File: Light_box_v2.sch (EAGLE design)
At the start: 35 parts, among them IC1 ATMEGA328-PU, U1 OPA1671IDBVR

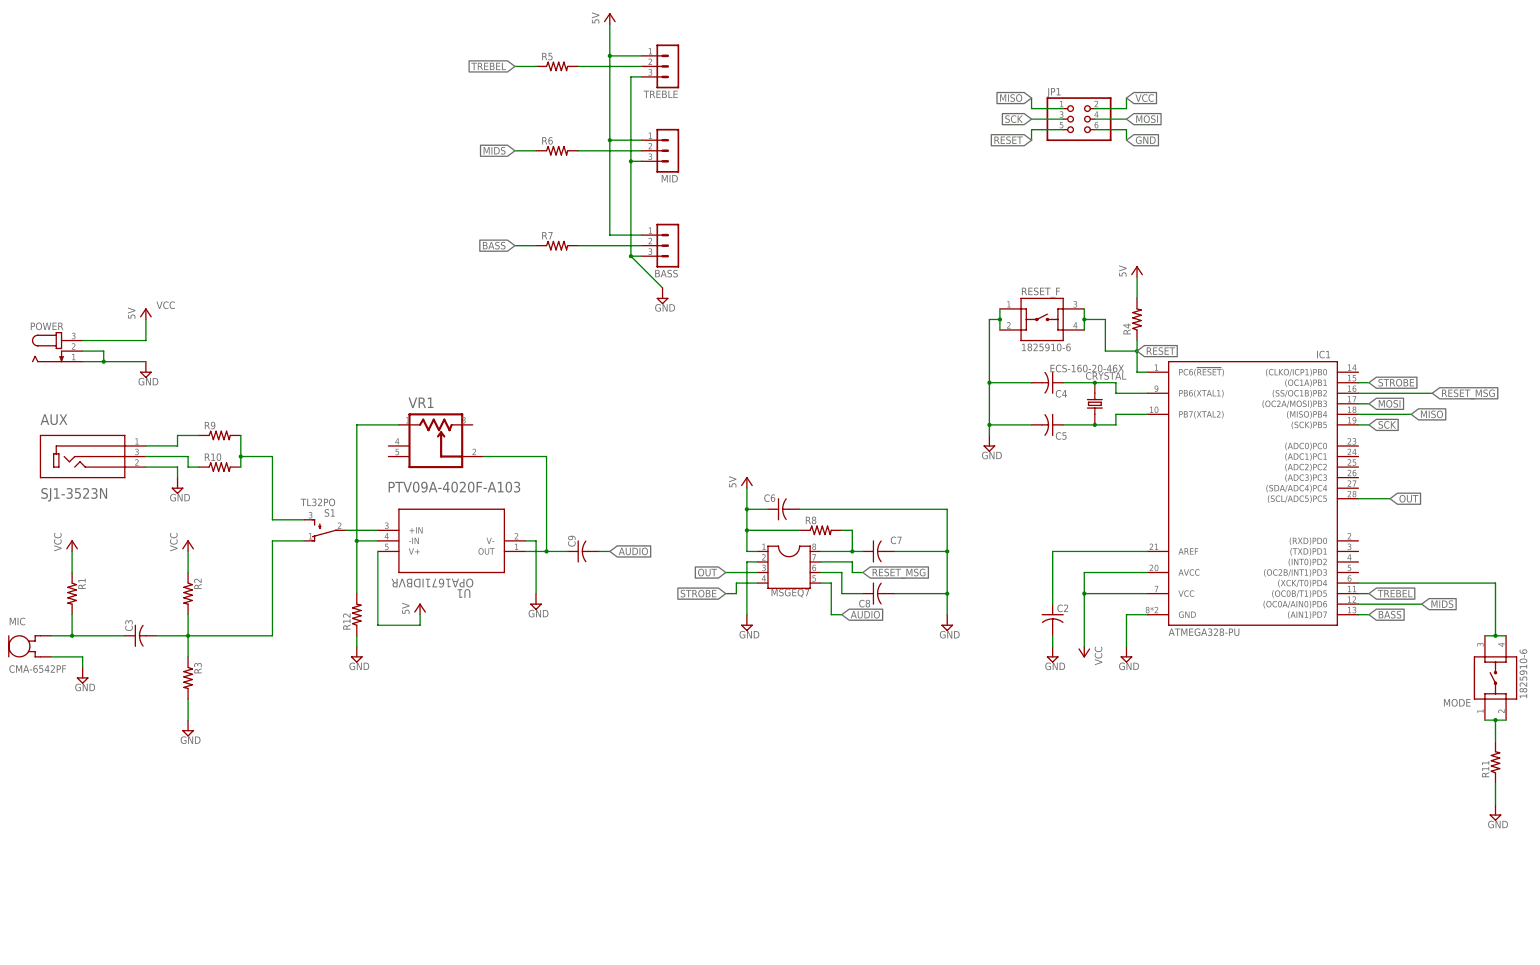
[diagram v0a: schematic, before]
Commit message: Adding some datasheets. Corrected error in mode button and added values to components
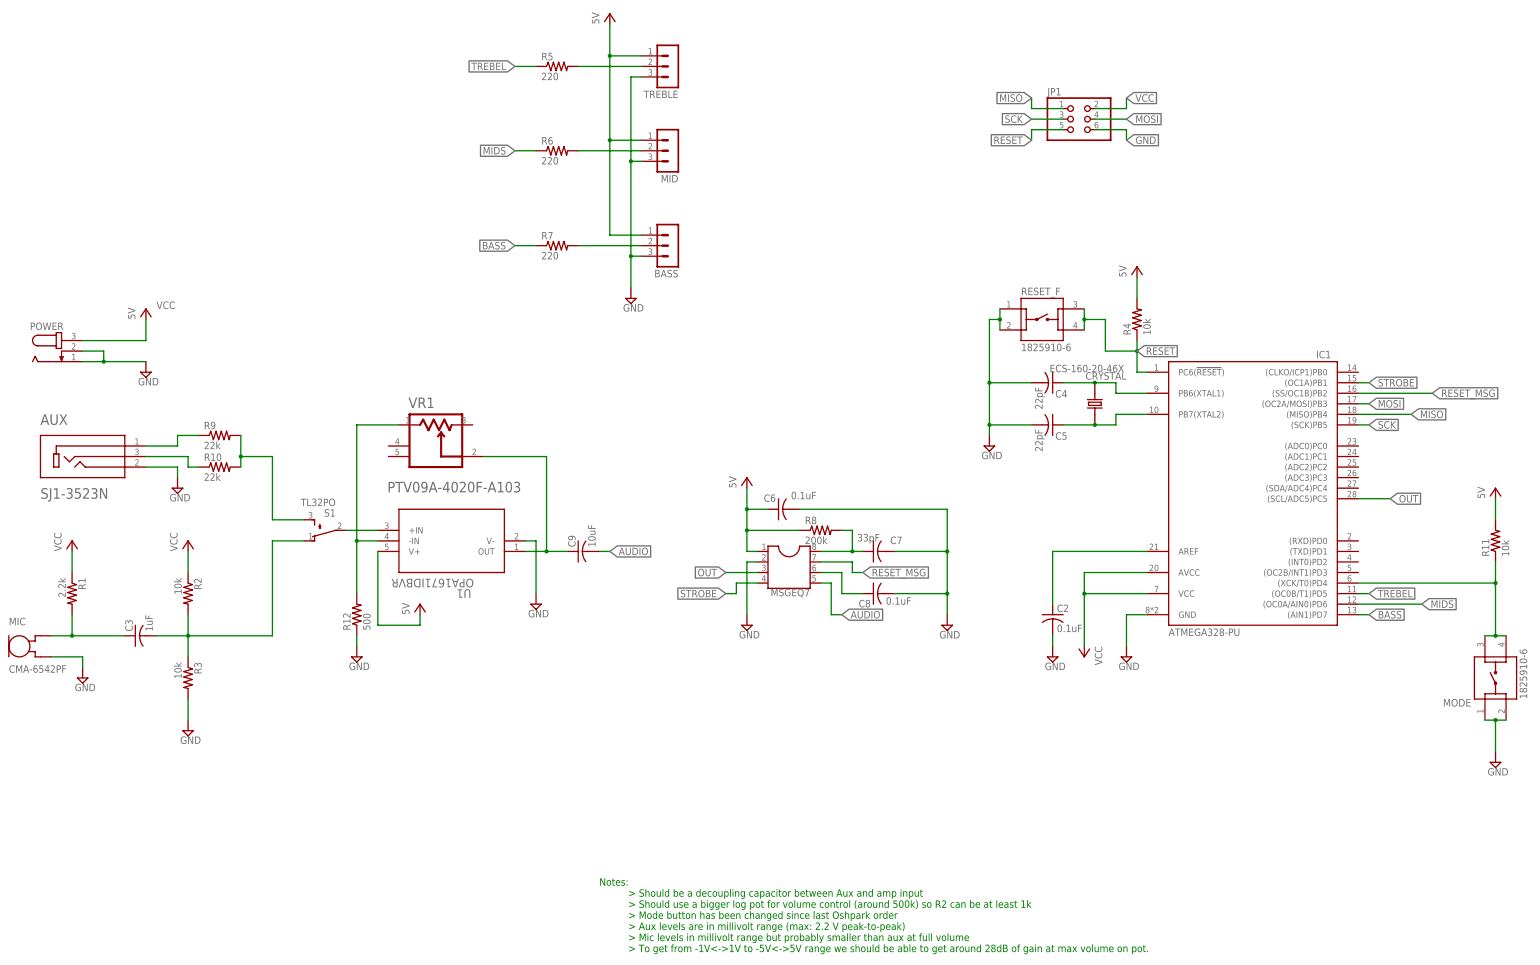
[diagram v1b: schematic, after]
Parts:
- C2, C6, C8: value (none) -> 0.1uF
- C3: value (none) -> 1uF
- C4, C5: value (none) -> 22pF
- C7: value (none) -> 33pF
- C9: value (none) -> 10uF
- R1: value (none) -> 2.2k
- R10, R9: value (none) -> 22k
- R11, R2, R3, R4: value (none) -> 10k
- R12: value (none) -> 500
- R5, R6, R7: value (none) -> 220
- R8: value (none) -> 200k
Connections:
- removed net N$17: MODE.1, MODE.2, R11.2
- net GND: now also MODE.1, MODE.2; no longer R11.1
- net N$22: now also R11.1
- net VCC: now also R11.2
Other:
- note added: "Notes: > Should be a decoupling capacitor between Aux and amp input > Should use a bigger log pot for volume control (around 500k) so R2 can be at least 1k > Mode button has been changed since last Oshpark order > Aux levels are in millivolt range (max: 2.2 V peak-to-peak) > Mic levels in millivolt range but probably smaller than aux at full volume > To get from -1V<->1V to -5V<->5V range we shou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"
- moved on the sheet: R11
